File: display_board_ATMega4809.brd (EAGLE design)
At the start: 53.3 x 120.3 mm, 38 parts, among them J2 LD09P33E4GV00LF, J3 SULLINS_NREC005SABC-M30RCSULL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, SW1 TE_CONNECTIVITY_FSM2JSMAATE_C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, SW2 TE_CONNECTIVITY_FSM2JSMAATE_C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, SW3 TE_CONNECTIVITY_FSM2JSMAATE_C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, SW4 TE_CONNECTIVITY_FSM2JSMAATE_C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, U1 LSF0102DCTR, U2 MCP1703AT-5002E_CB, U3 MCP1801T-3302I_OT, U5 ATMEGA4809-AU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

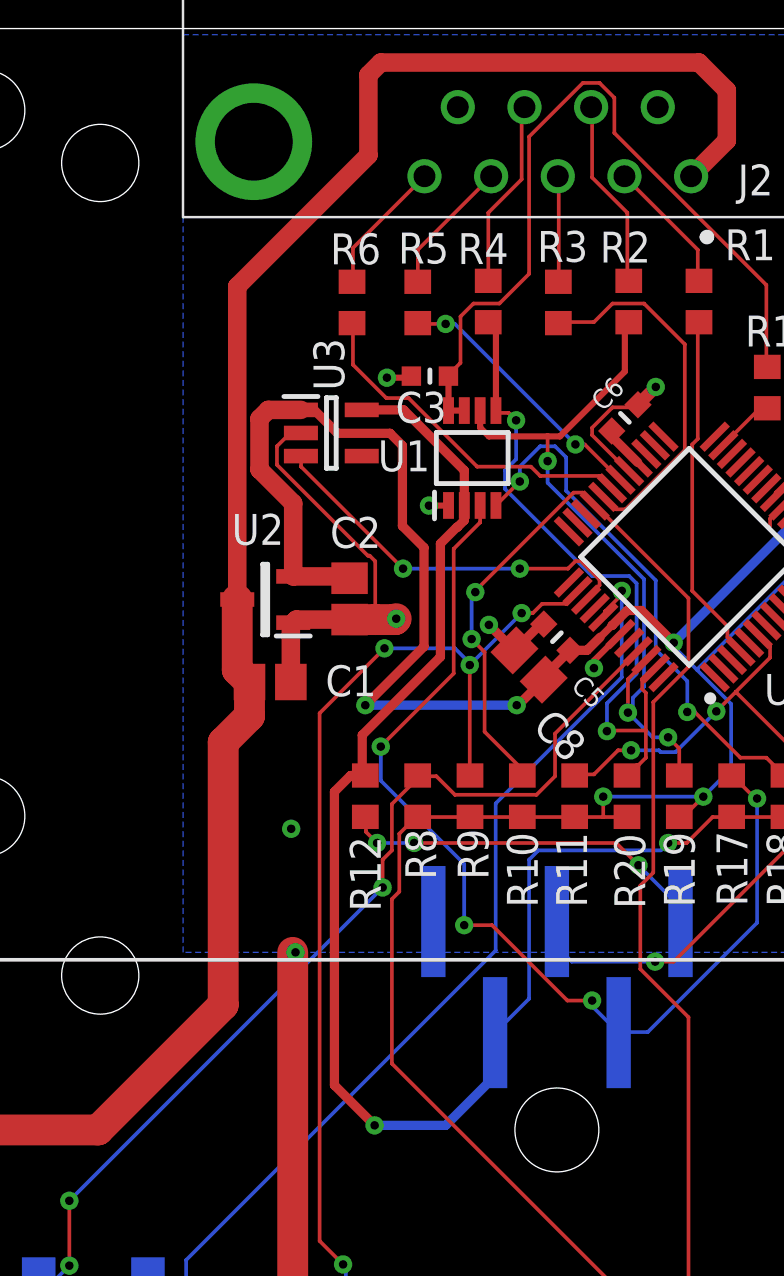
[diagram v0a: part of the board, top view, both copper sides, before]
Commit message: Adding decoupling capacitors
-Added decoupling capacitors on OLED LDO
-Added BOM file
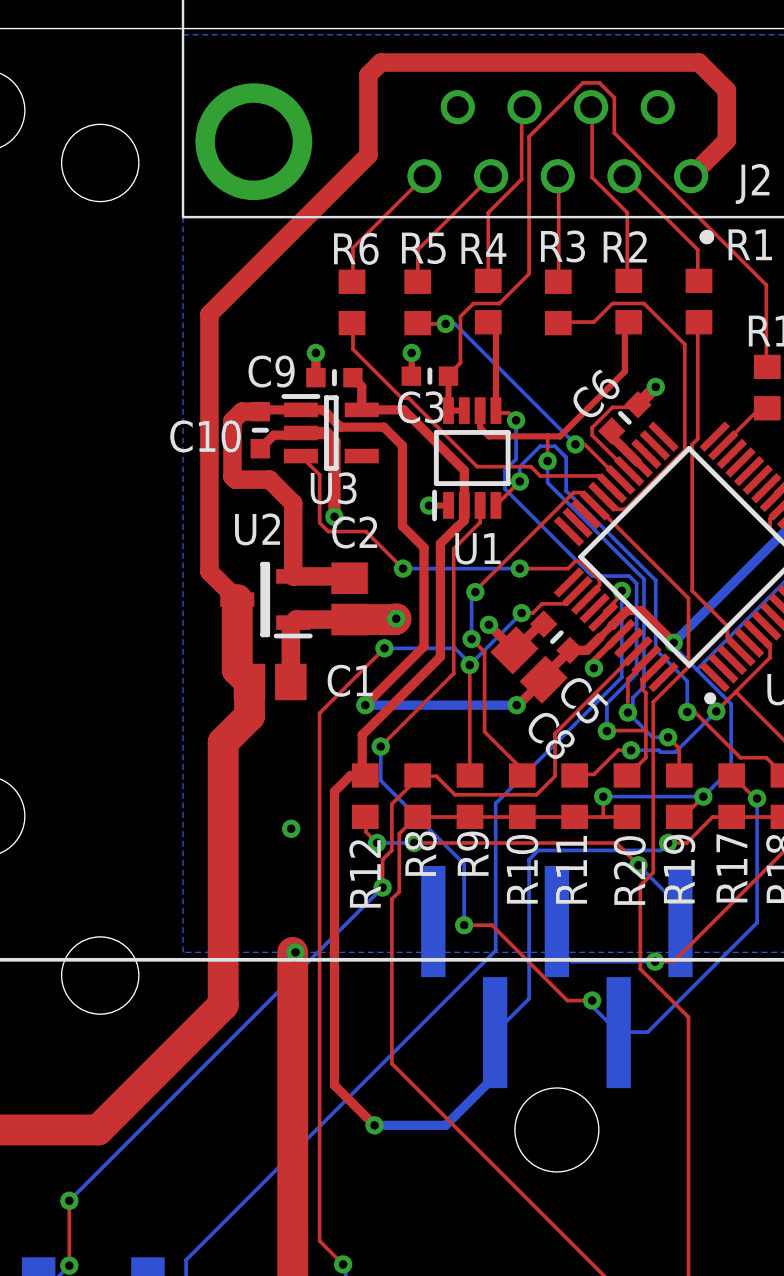
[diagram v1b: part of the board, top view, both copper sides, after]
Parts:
- added C10, C9: 0.1uF, microbuilder:_0603MP
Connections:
- net +3V3: now also C9.2
- net +5V: now also C10.2
- net GND: now also C10.1, C9.1
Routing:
- net +5V: track 178.3 -> 180.6 mm
- net GND: track 222.2 -> 219.9 mm, vias 13 -> 15
- net +3V3: track 62.0 -> 63.5 mm
- net VBAT: track 72.8 -> 73.8 mm
- net DISPLAY_SWITCH: track 15.9 -> 16.8 mm
